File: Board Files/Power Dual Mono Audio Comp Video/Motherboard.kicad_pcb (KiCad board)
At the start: 2 copper layers, 64 x 56 mm, 17 parts, among them J3 , J4 Video, J5 R Audio, J6 L Audio, P6 MOD RF, Q4 BC817, U12 L7805

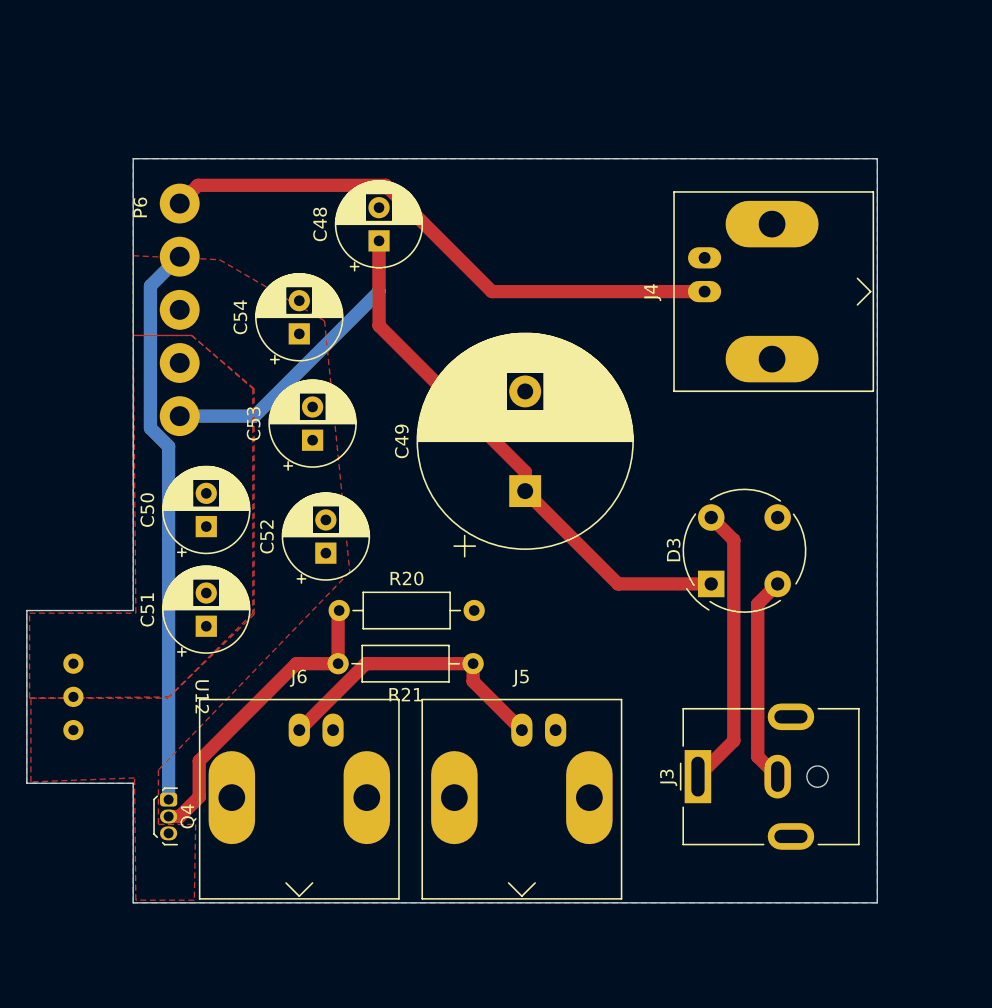
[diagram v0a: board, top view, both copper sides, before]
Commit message: Added board with built in AV/Power
Added board option with built in AV/Power and corrected the old oversized RCA place holders with accurate footprints.

Nothing is tested at this point but some quick eye math tells me that both boards can be combined.
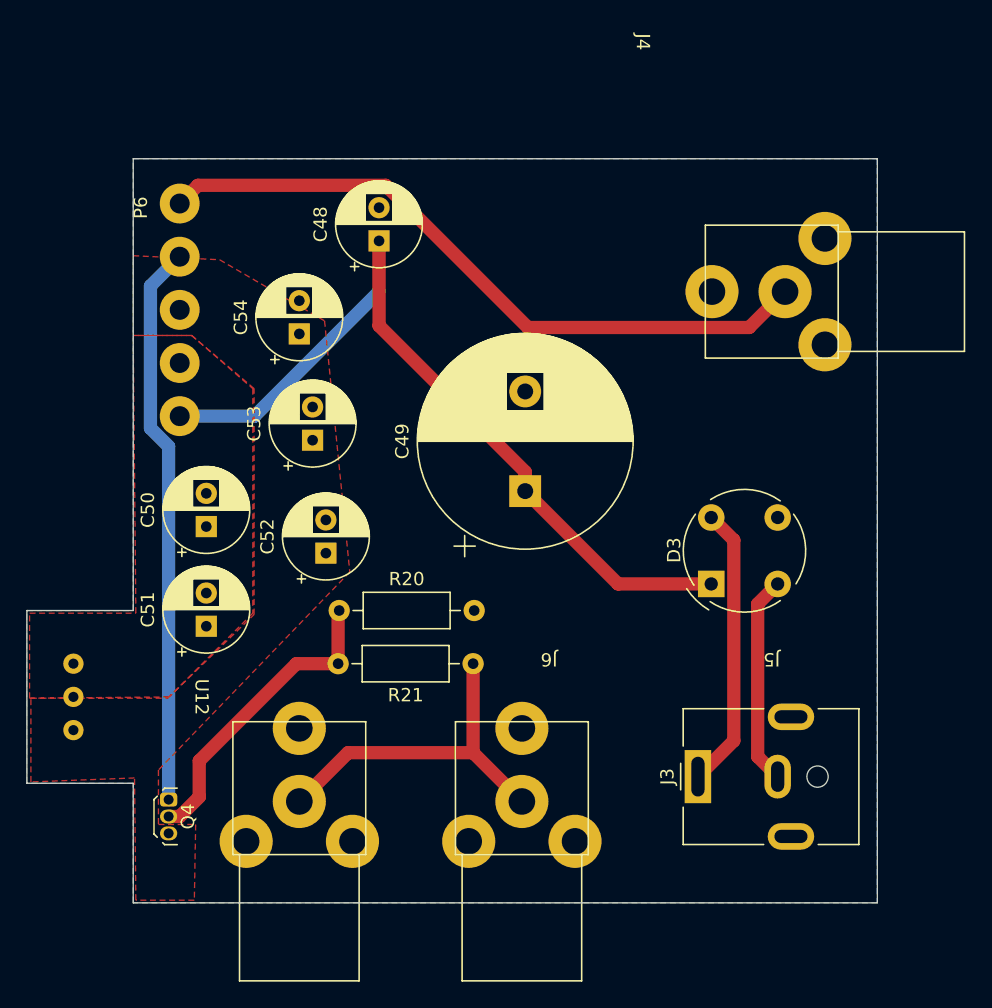
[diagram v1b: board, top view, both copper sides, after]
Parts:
- J4, J5, J6: footprint Connector_Coaxial:BNC_Amphenol_B6252HB-NPP3G-50_Horizontal -> NESRE:RCA
- moved J4 6.06 mm to (175.0, 67.6)
- moved J5 5.37 mm to (155.2, 106.0)
- moved J6 5.37 mm to (138.4, 106.0)
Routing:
- net /RF_Video: track 43.4 -> 51.7 mm
- net Net-(J5-Pad1): track 21.7 -> 26.5 mm
